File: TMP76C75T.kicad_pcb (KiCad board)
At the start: 2 copper layers, 116.8 x 91.4 mm, 48 parts, among them J1 Conn_01x08_Male, J2 Conn_01x07_Male, J3 Conn_01x08_Male, J3-2 Conn_01x08_Male, J4 Conn_01x08_Male, J4-2 Conn_01x08_Male, J5 Conn_01x08_Male, J6 Conn_01x06_Male, J7 Conn_01x08_Male, SW1 SW_DIP_x03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

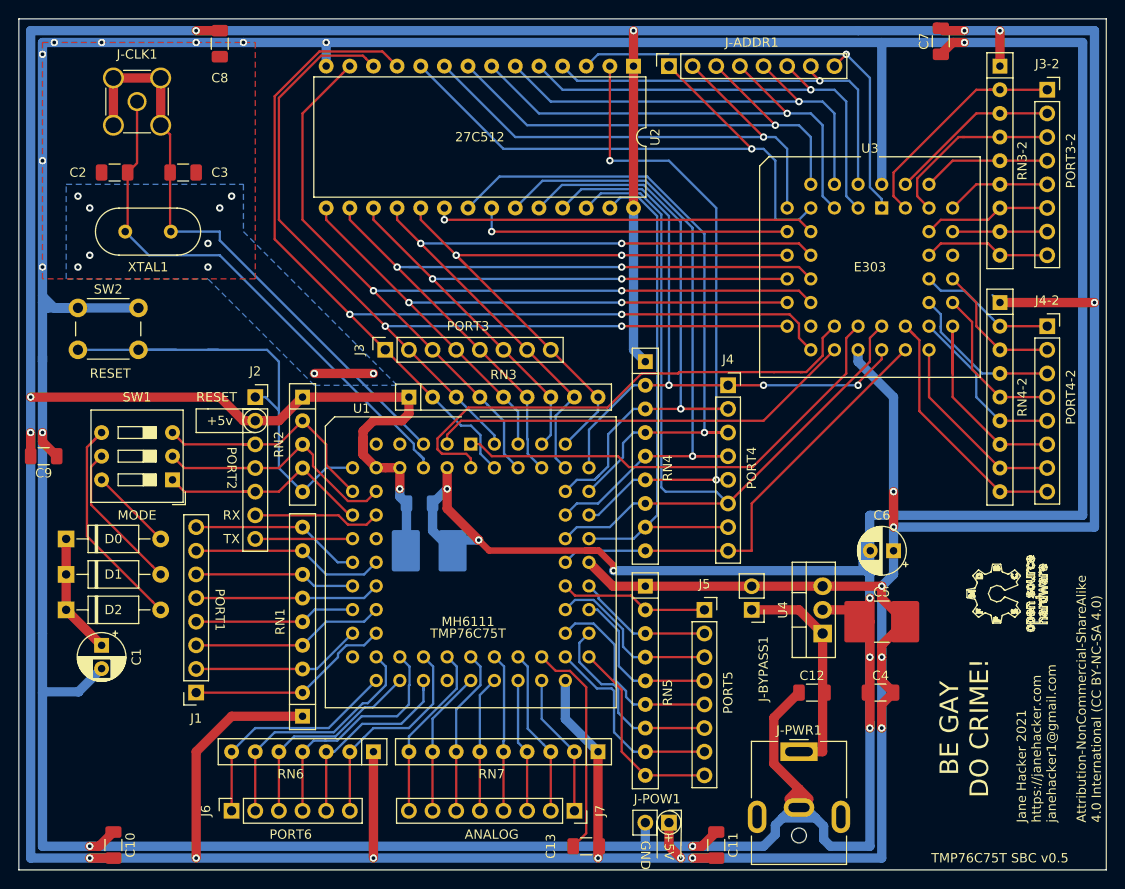
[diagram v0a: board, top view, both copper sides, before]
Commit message: Added via labels
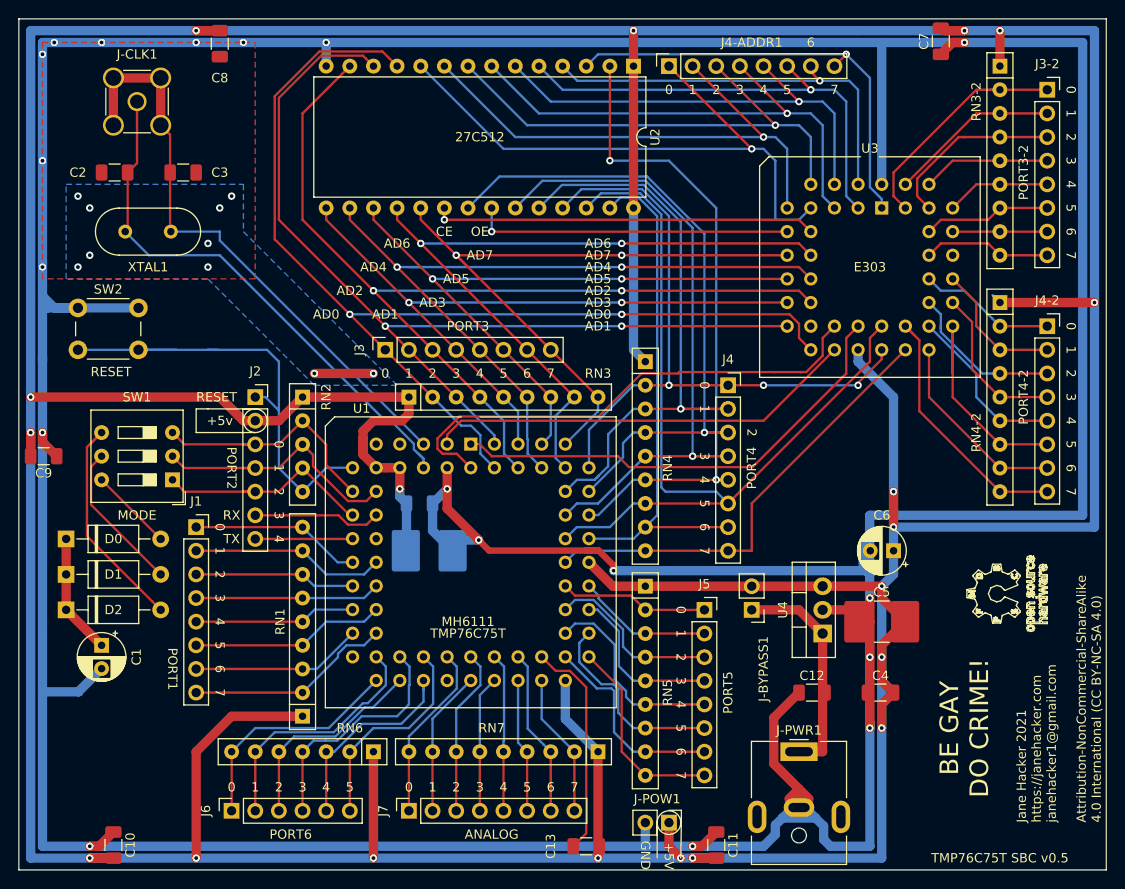
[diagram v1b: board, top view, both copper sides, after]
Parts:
- moved J1 17.8 mm to (102.9, 106.7), turned to 0 degrees
- moved J7 17.8 mm to (125.7, 137.2), turned to 90 degrees
- renumbered J-ADDR1 to J4-ADDR1
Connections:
- net Net-(C13-Pad1) renamed /AN-
- net Net-(U2-Pad20) renamed /CE
- net Net-(U2-Pad22) renamed /OE
- J1 pad 1: /P1.7 -> /P1.0
- J1 pad 2: /P1.6 -> /P1.1
- J1 pad 3: /P1.5 -> /P1.2
- J1 pad 4: /P1.4 -> /P1.3
- J1 pad 5: /P1.3 -> /P1.4
- J1 pad 6: /P1.2 -> /P1.5
- J1 pad 7: /P1.1 -> /P1.6
- J1 pad 8: /P1.0 -> /P1.7
- J7 pad 1: /P7.7 -> /P7.0
- J7 pad 2: /P7.6 -> /P7.1
- J7 pad 3: /P7.5 -> /P7.2
- J7 pad 4: /P7.4 -> /P7.3
- J7 pad 5: /P7.3 -> /P7.4
- J7 pad 6: /P7.2 -> /P7.5
- J7 pad 7: /P7.1 -> /P7.6
- J7 pad 8: /P7.0 -> /P7.7
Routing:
- net /AS: track 55.2 -> 54.6 mm
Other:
- board text added: "0"
- board text added: "1"
- board text added: "2"
- board text added: "3"
- board text added: "4"
- board text added: "5"
- board text added: "6"
- board text added: "7"
- board text added: "AD0"
- board text added: "AD1"
- board text added: "AD2"
- board text added: "AD3"
- board text added: "AD4"
- board text added: "AD5"
- board text added: "AD6"
- board text added: "AD7"
- board text added: "CE"
- board text added: "OE"
